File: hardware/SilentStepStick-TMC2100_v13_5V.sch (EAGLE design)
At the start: 30 parts, among them IC1 TMC2100-LA, X1 PASSER-07, X2 PASSER-07

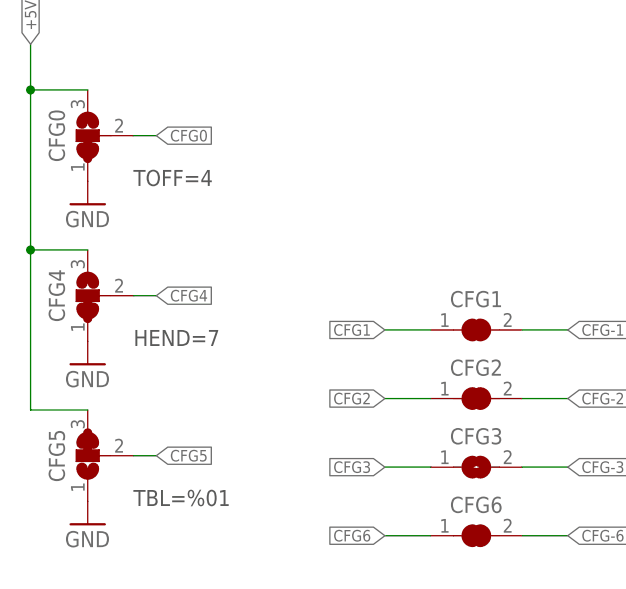
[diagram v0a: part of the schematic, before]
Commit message: updated schematics
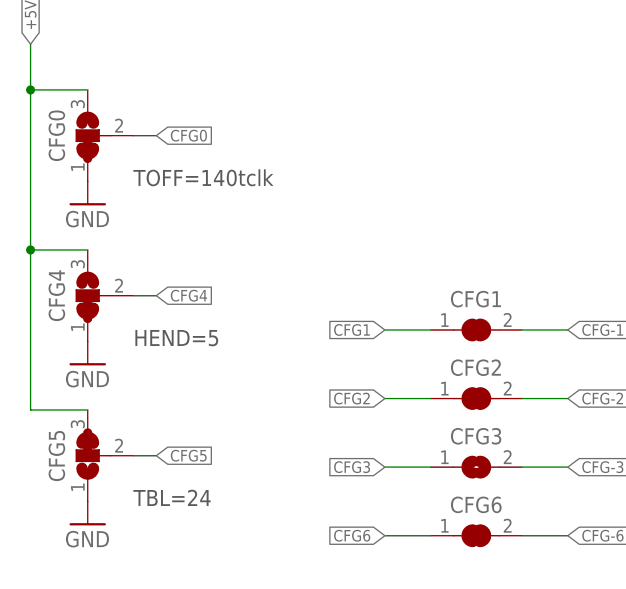
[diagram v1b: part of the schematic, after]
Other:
- note added: "HEND=5"
- note added: "TBL=24"
- note added: "TOFF=140tclk"
- note removed: "HEND=7"
- note removed: "TBL=%01"
- note removed: "TOFF=4"
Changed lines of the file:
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@@
 <wire x1="59.055" y1="24.13" x2="60.325" y2="24.13" width="1.016" layer="94"/>
 <wire x1="16.51" y1="50.8" x2="16.51" y2="53.34" width="1.016" layer="94"/>
-<text x="21.59" y="49.53" size="1.778" layer="97" font="vector" ratio="10" align="top-left">TOFF=4</text>
-<text x="21.59" y="31.75" size="1.778" layer="97" font="vector" ratio="10" align="top-left">HEND=7</text>
-<text x="21.59" y="13.97" size="1.778" layer="97" font="vector" ratio="10" align="top-left">TBL=%01</text>
+<text x="21.59" y="49.53" size="1.778" layer="97" font="vector" ratio="10" align="top-left">TOFF=140tclk</text>
+<text x="21.59" y="31.75" size="1.778" layer="97" font="vector" ratio="10" align="top-left">HEND=5</text>
+<text x="21.59" y="13.97" size="1.778" layer="97" font="vector" ratio="10" align="top-left">TBL=24</text>
 </plain>
 <instances>
